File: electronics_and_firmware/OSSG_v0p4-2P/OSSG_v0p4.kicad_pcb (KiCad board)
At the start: 4 copper layers, 85 x 9 mm, 82 parts, among them J1 Conn_01x05_Male, J2 USB_B_Micro, Q1 2SC4617R BR, Q2 2SC4617R BR, Q3 PMZ290UNE2YL, Q4 EMF20B02V, SW1 SW_SPST, SW2 Power, U1 SPH0645LMH, U2 ESP32-PICO-D4, U3 CH9102F, U4 XC61CC3002MR, U5 MP2615CGQ-Z, U6 H7650-50PR, U7 NCP167BMX330TBG

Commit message: started work on PCB layout
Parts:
- removed C20: 1uF, Capacitor_SMD:C_0402_1005Metric
- removed D4: WS2812C-2020, OSSG_footprints:LED_WS2812C-2020
- removed D5, D6: LED, Diode_SMD:D_0402_1005Metric
- removed D7: RB160M-30, Diode_SMD:D_SOD-123
- removed JP1: SolderJumper_2_Open, OSSG_footprints:JUMPER-2Psml_Open_RoundedPad2x1mm
- removed R14: 160K, Resistor_SMD:R_0402_1005Metric
- removed R15, R19: 884K, Resistor_SMD:R_0402_1005Metric
- removed R16: 320K, Resistor_SMD:R_0402_1005Metric
- removed R17: .025, Resistor_SMD:R_0402_1005Metric
- removed R18, R20: 100K, Resistor_SMD:R_0402_1005Metric
- removed TH1: 10K, Connector_PinHeader_1.27mm:PinHeader_1x02_P1.27mm_Horizontal
- added J3: USB_B_Micro, Connector_USB:USB_Micro-B_Amphenol_10118194_Horizontal, F.Cu at (131.7, 81.3)
- added L1: 1.5uH, OSSG_footprints:1.5uH_YXMAA0402-1R5M-ANP, F.Cu at (140.3, 87.3)
- added TP18: BATT2-, OSSG_footprints:Breakout_pads, B.Cu at (156.5, 76.2)
- added TP19: 5V, OSSG_footprints:Breakout_pads_small, F.Cu at (148.4, 88.3)
- added U8: SY7088, Package_DFN_QFN:DFN-8-1EP_3x2mm_P0.5mm_EP1.7x1.4mm, F.Cu at (145.3, 89.3)
- C13: value 1uF/16V -> 100nF
- C14: value 1uF/16V -> 22uF/16V
- C15: value 100nF/16V -> 1uF
- C16: value 22uF/16V -> 100nF
- C17, C19: value 1uF -> 22uF
- C18: value 10uF -> 1uF
- D1: moved to B.Cu
- D2: value WS2812C-2020 -> Red; footprint OSSG_footprints:LED_WS2812C-2020 -> Diode_SMD:D_0402_1005Metric
- D3: value WS2812C-2020 -> RB160M-30; footprint OSSG_footprints:LED_WS2812C-2020 -> Diode_SMD:D_SOD-123
- J1: footprint Connector_PinHeader_1.00mm:PinHeader_1x05_P1.00mm_Horizontal -> Connector_PinHeader_1.00mm:PinHeader_1x05_P1.00mm_Vertical
- J2: value USB_B_Micro -> Ext RGB; footprint Connector_USB:USB_Micro-B_Amphenol_10118194_Horizontal -> Connector_PinHeader_1.00mm:PinHeader_1x03_P1.00mm_Vertical; moved to F.Cu
- Q4: footprint Package_TO_SOT_SMD:SOT-23-6 -> OSSG_footprints:EMF20B02V
- R10: value 100K -> 1M
- R11: value 442K -> 1M
- R12: value 442K -> 470K
- R13: value 160K -> 147K
- R7: value 10K -> 2K
- R8: value 2K -> 150
- R9: value 2K -> 100K
- TP1, TP10, TP11, TP2, TP3, TP4, TP6, TP7: moved to F.Cu
- TP12, TP5: footprint TestPoint:TestPoint_Pad_D1.0mm -> OSSG_footprints:Breakout_pads_small
- TP13, TP14: footprint TestPoint:TestPoint_Pad_D1.0mm -> OSSG_footprints:Breakout_pads_small; moved to F.Cu
- TP15: value Batt+ -> Batt1+
- TP16: value GND -> Batt2+
- TP17: value BattMid -> BATT1-
- TP8, TP9: footprint OSSG_footprints:Breakout_pads -> OSSG_footprints:Breakout_pads_small; moved to F.Cu
- U5: value MP2615CGQ-Z -> AP5054HTC; footprint OSSG_footprints:MP2615GQ-P -> Package_TO_SOT_SMD:SOT-23-6
- U6: value H7650-50PR -> MAX17048; footprint Package_TO_SOT_SMD:SOT-89-3 -> Package_DFN_QFN:DFN-8-1EP_2x2mm_P0.5mm_EP0.8x1.6mm
- moved TP13 81.6 mm to (76.1, 92.3), turned to 0 degrees
- moved TP14 78.7 mm to (79.2, 89.3), turned to 0 degrees
- moved U6 71.6 mm to (156.2, 77.5)
- moved R7 67.4 mm to (152.6, 80.2), turned to 180 degrees
- moved C15 66.4 mm to (148.8, 90.4)
- moved R1 64.8 mm to (86.0, 79.7), turned to 0 degrees
- moved C16 62.4 mm to (146.1, 87.4), turned to 180 degrees
- moved R6 61.8 mm to (148.0, 80.4), turned to 0 degrees
- moved D1 60.9 mm to (79.4, 76.7), turned to 0 degrees
- moved TP12 59.6 mm to (84.6, 89.3)
- moved TP5 59.6 mm to (81.5, 89.3)
- moved R3 55.3 mm to (96.7, 78.4)
- moved J1 52.3 mm to (79.6, 82.7), turned to 180 degrees
- moved TP4 49.3 mm to (74.0, 92.2), turned to 0 degrees
- moved J2 47.9 mm to (76.5, 76.2), turned to 0 degrees
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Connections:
- net IO4 renamed RGB
- C12 pad 1: BATT1- -> BATT+
- C13 pad 1: Net-(C13-Pad1) -> BATT+
- C14 pad 1: Net-(C14-Pad1) -> BATT+
- C15 pad 2: Net-(C15-Pad2) -> BATT2-
- C16 pad 1: BATT+ -> +5V
- C17 pad 1: V_PSU -> Net-(C15-Pad1)
- C18 pad 1: +5V -> BATT2-
- C18 pad 2: BATT2- -> +3V3
- C19 pad 1: BATT2- -> +5V
- C19 pad 2: V_PSU -> BATT2-
- D2 pad 2: BATT2- -> VBUS
- D3 pad 1: Net-(D3-Pad1) -> Net-(C15-Pad1)
- D3 pad 2: BATT2- -> VBUS
- J2 pad 1: V_USB -> BATT2-
- J2 pad 2: USB- -> Net-(D1-Pad1)
- J2 pad 3: USB+ -> +5V
- Q3 pad 1: PSEN -> Net-(Q3-Pad1)
- Q4 pad 3: V_PSU -> Net-(C15-Pad1)
- Q4 pad 4: V_USB -> VBUS
- R10 pad 1: BATT2- -> Net-(Q3-Pad3)
- R10 pad 2: Net-(R10-Pad2) -> BATT+
- R11 pad 1: BATT+ -> BATT2-
- R11 pad 2: Net-(R11-Pad2) -> VBUS
- R12 pad 1: Net-(R11-Pad2) -> Net-(R12-Pad1)
- R12 pad 2: ADC1C2 -> +5V
- R13 pad 1: ADC1C2 -> BATT2-
- R13 pad 2: Net-(R13-Pad2) -> Net-(R12-Pad1)
- R6 pad 1: BATT1- -> BATT+
- R7 pad 1: Net-(C13-Pad1) -> BATT2-
- R8 pad 1: Net-(D6-Pad1) -> PSEN
- R8 pad 2: Net-(R8-Pad2) -> Net-(Q3-Pad1)
- R9 pad 1: Net-(D5-Pad1) -> BATT2-
- R9 pad 2: Net-(R9-Pad2) -> Net-(Q3-Pad1)
- TP11 pad 1: IO18 -> unconnected-(TP11-Pad1)
- TP16 pad 1: BATT2- -> BATT+
- TP17 pad 1: BATT1- -> BATT2-
- TP2 pad 1: IO26 -> unconnected-(TP2-Pad1)
- TP6 pad 1: IO32 -> unconnected-(TP6-Pad1)
- U4 pad 3: BATT1- -> BATT+
- U5 pad 1: Net-(C15-Pad2) -> Net-(D2-Pad1)
- U5 pad 2: V_USB -> BATT2-
- U5 pad 3: Net-(R7-Pad2) -> BATT+
- U5 pad 4: Net-(JP1-Pad1) -> VBUS
- U5 pad 6: Net-(R10-Pad2) -> Net-(R7-Pad2)
- U6 pad 2: V_PSU -> BATT+
- U6 pad 3: +5V -> BATT+
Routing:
- net BATT2-: track 442.0 -> 0.01 mm, vias 73 -> 16
- net IO33: track 15.9 -> 0.00 mm, vias 2 -> 0
- net EN: track 15.0 -> 0.00 mm, vias 2 -> 0
- net ADC1C0: track 12.3 -> 0.00 mm, vias 1 -> 0
- net IO14: track 12.0 -> 0.00 mm, vias 3 -> 0
- net IO32: track 11.8 -> 0.00 mm, vias 3 -> 0
- net USB-: track 10.5 -> 0.00 mm
- net EXT1_MIC_DATA: track 9.77 -> 0.00 mm, vias 2 -> 0
- net IO5: track 6.86 -> 0.00 mm, vias 1 -> 0
- net Net-(R13-Pad2): track 5.83 -> 0.00 mm, vias 3 -> 0
- net ADC1C2: track 5.17 -> 0.00 mm, vias 2 -> 0
- net Net-(IC1-Pad3): track 4.96 -> 0.00 mm, vias 2 -> 0
- net Net-(C4-Pad1): track 4.69 -> 0.00 mm, vias 2 -> 0
- net Net-(IC1-Pad1): track 3.35 -> 0.00 mm
- net +3V3: track 3.19 -> 0.00 mm, vias 2 -> 0
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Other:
- outline, holes or cut-outs redrawn
- board text removed: "."

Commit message: V0.4-2P PCB nearly finished
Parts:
- removed TP11: IO18_BO, OSSG_footprints:Breakout_pads_small
- removed TP2: IO26_BO, OSSG_footprints:Breakout_pads_small
- removed TP6: IO32_BO, OSSG_footprints:Breakout_pads_small
- removed TP7: IO33_BO, OSSG_footprints:Breakout_pads_small
- added C20: 1uF, Capacitor_SMD:C_0402_1005Metric, F.Cu at (85.0, 77.9)
- added F1: 1A, Resistor_SMD:R_0805_2012Metric, F.Cu at (123.4, 76.9)
- added J4: Touch, OSSG_footprints:Solder-2P-Connector, B.Cu at (104.7, 84.4)
- added R14: 147K, Resistor_SMD:R_0402_1005Metric, F.Cu at (132.5, 76.1)
- C1: value 100nF -> 1uF
- C2: value 1uF -> 100nF
- C4: value 10uF -> 100nF
- C5: value 0.1uF -> 10uF
- J1: footprint Connector_PinHeader_1.00mm:PinHeader_1x05_P1.00mm_Vertical -> OSSG_footprints:Solder-5P-Connector; moved to B.Cu
- J2: footprint Connector_PinHeader_1.00mm:PinHeader_1x03_P1.00mm_Vertical -> OSSG_footprints:Solder-3P-Connector; moved to B.Cu
- R1: value 0R* -> 10K
- R10: value 1M -> 100K
- R12: value 470K -> 1M
- R13: value 147K -> 470K
- R3: value 10K -> 0R*
- R6: value 100k -> 10K
- R7: value 2K -> 100k
- R8: value 150 -> 2K
- R9: value 100K -> 150
- SW1: footprint Button_Switch_SMD:SW_SPST_B3U-3000P-B -> OSSG_footprints:SMD_Switch_Panasonic_EVQPUL_EVQPUC_6.3x6.7
- TP12: value IO0_TP -> IO0; footprint OSSG_footprints:Breakout_pads_small -> OSSG_footprints:Breakout_pads_very_small; moved to B.Cu
- TP13: value TXIN -> Tx; footprint OSSG_footprints:Breakout_pads_small -> OSSG_footprints:Breakout_pads_very_small; moved to B.Cu
- TP14: value RXIN -> Rx; footprint OSSG_footprints:Breakout_pads_small -> OSSG_footprints:Breakout_pads_very_small; moved to B.Cu
- TP19: moved to B.Cu
- TP5: footprint OSSG_footprints:Breakout_pads_small -> OSSG_footprints:Breakout_pads_very_small; moved to B.Cu
- TP8: value +3.3V_BO -> 3V3; moved to B.Cu
- TP9: value GND_BO -> GND; moved to B.Cu
- U1: value SPH0645LMH -> MP23DB01HPTR; footprint OSSG_footprints:SPH0645LM4H-B-SMD-GND -> OSSG_footprints:MP23DB01HPTR
- moved R4 47.4 mm to (77.0, 79.7)
- moved R6 40.7 mm to (107.2, 79.6), turned to 90 degrees
- moved TP13 34.6 mm to (107.3, 77.2), turned to 180 degrees
- moved TP14 30.4 mm to (106.6, 76.0), turned to 180 degrees
- moved C4 30.4 mm to (78.8, 79.7), turned to 0 degrees
- moved SW2 28.7 mm to (113.7, 80.3), turned to 0 degrees
- moved TP4 28.2 mm to (101.7, 87.4)
- moved C16 27.9 mm to (120.4, 76.6), turned to -90 degrees
- moved TP5 26.5 mm to (106.8, 81.1), turned to 180 degrees
- moved TP12 26.3 mm to (110.0, 82.5), turned to 180 degrees
- moved C15 22.9 mm to (130.1, 77.1), turned to 90 degrees
- moved C18 21.2 mm to (117.9, 76.6), turned to -90 degrees
- moved R13 21.1 mm to (131.1, 76.5), turned to 90 degrees
- moved TP1 20.4 mm to (104.3, 87.4)
- moved TP19 20.0 mm to (132.3, 76.4)
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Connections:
- C1 pad 1: +3V3 -> EN
- C2 pad 1: EN -> +3V3
- C4 pad 1: Net-(C4-Pad1) -> SWITCH
- C5 pad 1: Net-(C4-Pad1) -> +3V3
- C6 pad 1: ADC1C0 -> +3V3
- C7 pad 1: ADC1C1 -> ADC1C0
- C8 pad 1: ADC1C2 -> ADC1C1
- J1 pad 3: IO21 -> i2S2_CLK
- J1 pad 4: IO23 -> i2S2_Data
- J1 pad 5: IO9 -> i2S2_WS
- J3 pad 1: VBUS -> Net-(J3-Pad1)
- Q4 pad 5: Net-(Q4-Pad5) -> Net-(Q4-Pad6)
- Q4 pad 7: Net-(Q4-Pad5) -> Net-(Q4-Pad6)
- R1 pad 1: Net-(R1-Pad1) -> EN
- R10 pad 1: Net-(Q3-Pad3) -> BATT2-
- R10 pad 2: BATT+ -> Net-(Q3-Pad1)
- R11 pad 1: BATT2- -> Net-(Q3-Pad3)
- R11 pad 2: VBUS -> BATT+
- R12 pad 1: Net-(R12-Pad1) -> BATT2-
- R12 pad 2: +5V -> VBUS
- R13 pad 1: BATT2- -> Net-(R13-Pad1)
- R13 pad 2: Net-(R12-Pad1) -> +5V
- R2 pad 1: BATT2- -> Net-(R2-Pad1)
- R2 pad 2: Net-(R1-Pad1) -> +3V3
- R3 pad 1: EN -> BATT2-
- R3 pad 2: +3V3 -> Net-(R2-Pad1)
- R4 pad 1: DTR -> SWITCH
- R4 pad 2: Net-(Q1-Pad1) -> +3V3
- R5 pad 1: RTS -> DTR
- R5 pad 2: Net-(Q2-Pad1) -> Net-(Q1-Pad1)
- R6 pad 1: BATT+ -> RTS
- R6 pad 2: PSEN -> Net-(Q2-Pad1)
- R7 pad 1: BATT2- -> BATT+
- R7 pad 2: Net-(R7-Pad2) -> PSEN
- R8 pad 1: PSEN -> BATT2-
- R8 pad 2: Net-(Q3-Pad1) -> Net-(R8-Pad2)
- R9 pad 1: BATT2- -> PSEN
- SW1 pad 1: BATT2- -> SWITCH
- SW1 pad 2: EN -> BATT2-
- U1 pad 1: IO33 -> i2S1_Data
- U1 pad 2: Net-(R1-Pad1) -> Net-(R2-Pad1)
- U1 pad 4: IO32 -> i2S1_CLK
- U1 pad 6: IO14 -> (no net)
- U2 pad 12: IO32 -> i2S2_WS
- U2 pad 13: IO33 -> i2S1_CLK
- U2 pad 14: IO25 -> i2S2_CLK
- U2 pad 15: IO26 -> i2S1_Data
- U2 pad 16: IO27 -> unconnected-(U2-Pad16)
- U2 pad 17: IO14 -> RGB
- U2 pad 22: IO2 -> TOUCH1
- U2 pad 24: RGB -> SDA
- U2 pad 35: IO18 -> SCL
- U2 pad 36: IO23 -> unconnected-(U2-Pad36)
- U2 pad 42: IO21 -> ALRT
- U2 pad 5: ADC1C2 -> SWITCH
- U2 pad 6: ADC1C0 -> unconnected-(U2-Pad6)
- U2 pad 8: IO39 -> i2S2_Data
- U5 pad 6: Net-(R7-Pad2) -> Net-(R8-Pad2)
- U6 pad 5: IO18 -> ALRT
- U6 pad 7: IO32 -> SCL
- U6 pad 8: IO26 -> SDA
- U8 pad 5: Net-(R12-Pad1) -> Net-(R13-Pad1)
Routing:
- net +5V: track 0.00 -> 77.1 mm, vias 0 -> 7
- net BATT2-: track 0.01 -> 76.0 mm, vias 16 -> 93
- net SCL: track 0.00 -> 60.8 mm, vias 0 -> 2
- net ALRT: track 0.00 -> 59.3 mm, vias 0 -> 2
- net SDA: track 0.00 -> 54.5 mm, vias 0 -> 2
- net VBUS: track 0.00 -> 53.5 mm, vias 0 -> 6
- net PSEN: track 0.00 -> 47.1 mm, vias 0 -> 4
- net BATT+: track 0.20 -> 33.5 mm, vias 0 -> 3
- net SWITCH: track 0.00 -> 27.0 mm, vias 0 -> 2
- net +3V3: track 0.00 -> 26.6 mm, vias 0 -> 17
- net Net-(C15-Pad1): track 0.00 -> 23.9 mm, vias 0 -> 2
- net RGB: track 0.00 -> 22.8 mm, vias 0 -> 3
- net USB+: track 0.00 -> 22.0 mm, vias 0 -> 2
- net USB-: track 0.00 -> 20.5 mm, vias 0 -> 2
- net i2S1_Data: track 0.00 -> 20.0 mm, vias 0 -> 2
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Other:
- outline, holes or cut-outs redrawn
- board text added: "+"
- board text added: "-"
- board text added: "3V3"
- board text added: "5V"
- board text added: "CLK"
- board text added: "D"
- board text added: "Din"
- board text added: "GND"
- board text added: "OFF"
- board text added: "ON"
- board text added: "Open Source Smart Glasses v0.4"
- board text added: "Power OFF<-->ON"
- board text added: "USB DATA POWER"
- board text added: "WS"
- board text removed: "Open Source Smart Glasses v0.3"

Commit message: EOD - PCB nearly finished
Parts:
- removed C7, C8: 0.1uF, Capacitor_SMD:C_0402_1005Metric
- removed TP10: IO5_BO, OSSG_footprints:Breakout_pads_small
- removed TP19: 5V, OSSG_footprints:Breakout_pads_small
- removed TP3: IO38_ADC1C1, OSSG_footprints:Breakout_pads_small
- removed TP4: IO37_ADC1C0, OSSG_footprints:Breakout_pads_small
- added R15: 10K, Resistor_SMD:R_0402_1005Metric, F.Cu at (132.9, 82.8)
- added R16: 10k, Resistor_SMD:R_0402_1005Metric, F.Cu at (134.0, 82.8)
- added R17: 10K, Resistor_SMD:R_0402_1005Metric, F.Cu at (135.0, 82.7)
- added R18: 100K, Resistor_SMD:R_0402_1005Metric, F.Cu at (120.6, 78.7)
- added TP2: 5V, OSSG_footprints:Breakout_pads_small, B.Cu at (132.2, 76.4)
- TP1: value IO25_BO -> IO35; footprint OSSG_footprints:Breakout_pads_small -> OSSG_footprints:Breakout_pads_very_small; moved to B.Cu
- moved TP1 8.68 mm to (97.9, 81.5), turned to 180 degrees
- moved TP13 0.09 mm to (107.2, 77.2)
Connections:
- net BATT+ renamed BATT1+
- net BATT2- renamed BATT1-
- C9 pad 2: V_USB -> VBUS
- SW2 pad 2: PSEN -> Net-(Q3-Pad1)
- SW2 pad 3: unconnected-(SW2-Pad3) -> Net-(SW2-Pad3)
- TP1 pad 1: IO25 -> SPARE
- U2 pad 10: IO34 -> unconnected-(U2-Pad10)
- U2 pad 11: IO35 -> SPARE
- U2 pad 18: IO12 -> unconnected-(U2-Pad18)
- U2 pad 20: IO13 -> unconnected-(U2-Pad20)
- U2 pad 21: IO15 -> unconnected-(U2-Pad21)
- U2 pad 28: IO9 -> unconnected-(U2-Pad28)
- U2 pad 34: IO5 -> unconnected-(U2-Pad34)
- U2 pad 38: IO19 -> unconnected-(U2-Pad38)
- U2 pad 39: IO22 -> unconnected-(U2-Pad39)
- U2 pad 7: ADC1C1 -> unconnected-(U2-Pad7)
- U3 pad 7: V_USB -> VBUS
- U3 pad 8: V_USB -> VBUS
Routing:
- net BATT1+: track 33.5 -> 53.5 mm, vias 3 -> 4
- net VBUS: track 53.5 -> 70.0 mm, vias 6 -> 7
- net +3V3: track 26.6 -> 29.8 mm, vias 17 -> 18
- net SDA: track 54.5 -> 57.0 mm, vias 2 -> 4
- net V_USB: track 2.05 -> 0.00 mm
- net SPARE: track 0.00 -> 1.69 mm, vias 0 -> 1
- net ALRT: track 59.3 -> 60.9 mm, vias 2 -> 3
- net SCL: track 60.8 -> 62.3 mm, vias 2 -> 3
- net Net-(SW2-Pad3): track 0.00 -> 1.23 mm
- net +5V: track 77.1 -> 78.0 mm
- net BATT1-: vias 93 -> 101
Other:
- outline, holes or cut-outs redrawn
- board text added: "Open Source Smart Glasses V0.4"
- board text removed: "Open Source Smart Glasses v0.4"

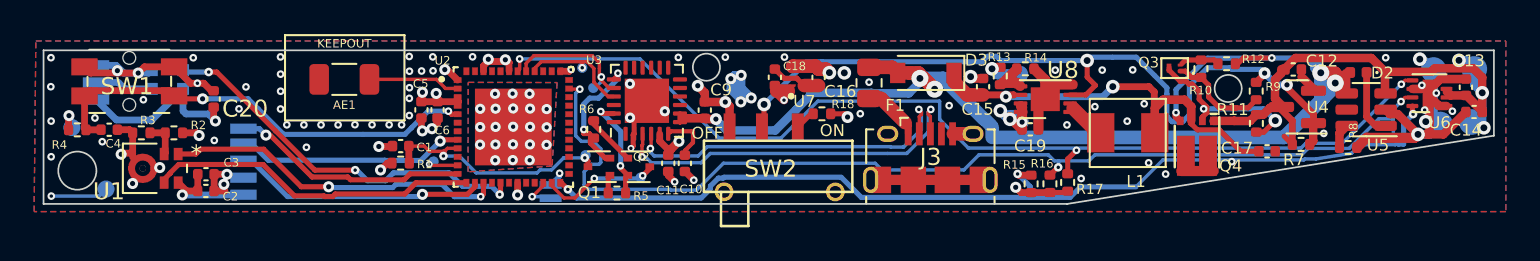
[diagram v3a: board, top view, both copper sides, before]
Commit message: V0.4 PCB nearly finished.  3D models mostly added in. Needs reviewing
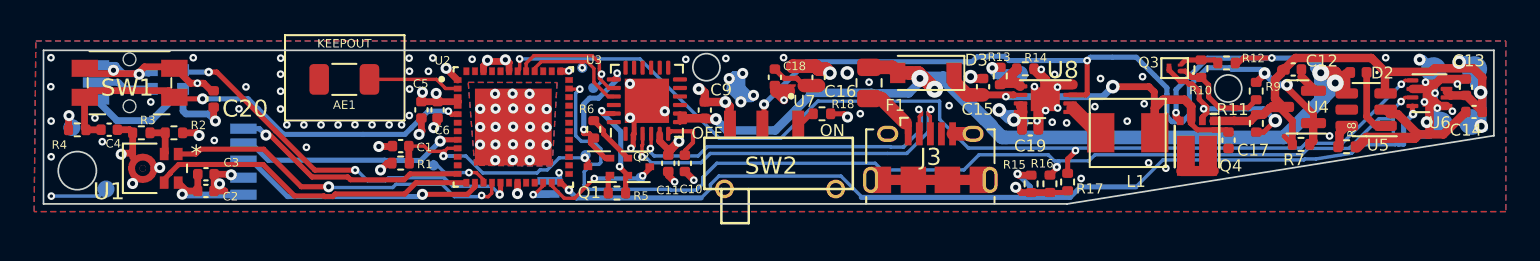
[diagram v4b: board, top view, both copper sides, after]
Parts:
- R18: value 100K -> 10K
- TP1: value IO35 -> IO26
- moved C17 2.35 mm to (144.4, 80.3), turned to -90 degrees
- moved J4 0.27 mm to (104.6, 84.1)
- moved TP1 0.23 mm to (97.9, 81.7)
- moved SW2 0.17 mm to (113.7, 80.1)
- moved R8 0.11 mm to (151.4, 80.7)
- moved SW1 0.08 mm to (80.0, 76.9)
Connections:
- net BATT1+ renamed BATT+
- SW2 pad 2: Net-(Q3-Pad1) -> PSEN
- TP1 pad 1: SPARE -> DAC
- U2 pad 15: i2S1_Data -> DAC
- U2 pad 16: unconnected-(U2-Pad16) -> i2S1_Data
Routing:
- net BATT+: track 53.5 -> 79.1 mm
- net DAC: track 0.00 -> 3.54 mm, vias 0 -> 1
- net +5V: track 78.0 -> 75.8 mm, vias 7 -> 6
- net Net-(C15-Pad1): track 23.9 -> 22.1 mm
- net SPARE: track 1.69 -> 0.00 mm, vias 1 -> 0
- net BATT1-: track 76.0 -> 77.1 mm, vias 101 -> 107
- net EN: track 14.0 -> 15.0 mm
- net TOUCH1: track 2.20 -> 3.08 mm
- net SDA: track 57.0 -> 57.2 mm, vias 4 -> 3

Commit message: finished board?
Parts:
- TP5: value EN_TP -> EN
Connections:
- SW2 pad 2: PSEN -> Net-(Q3-Pad1)
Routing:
- net +3V3: track 29.7 -> 39.2 mm
- net VBUS: track 69.6 -> 63.3 mm
- net PSEN: track 46.7 -> 42.1 mm
- net +5V: track 75.8 -> 75.1 mm
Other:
- board text added: "LED"
- board text added: "Power ON<-->OFF"
- board text added: "Touch"
- board text added: "i2S"
- board text removed: "Power OFF<-->ON"

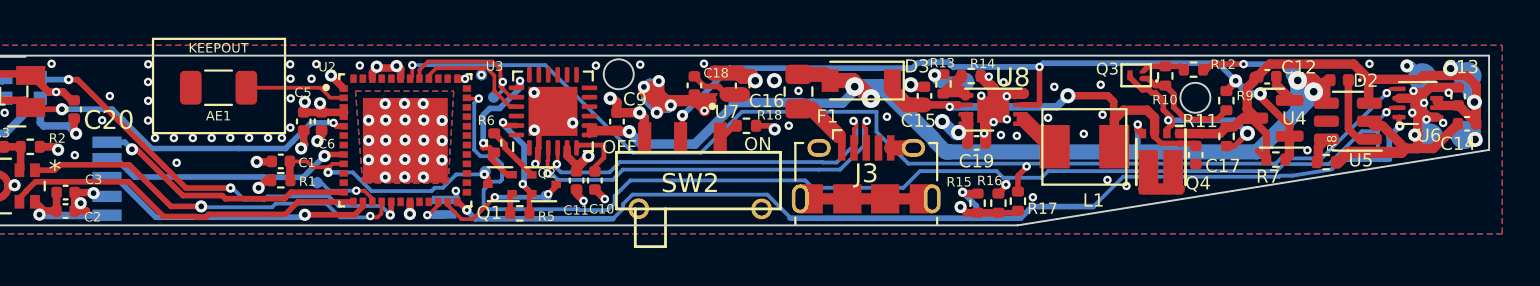
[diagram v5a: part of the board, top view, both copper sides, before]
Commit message: minor footprint updates
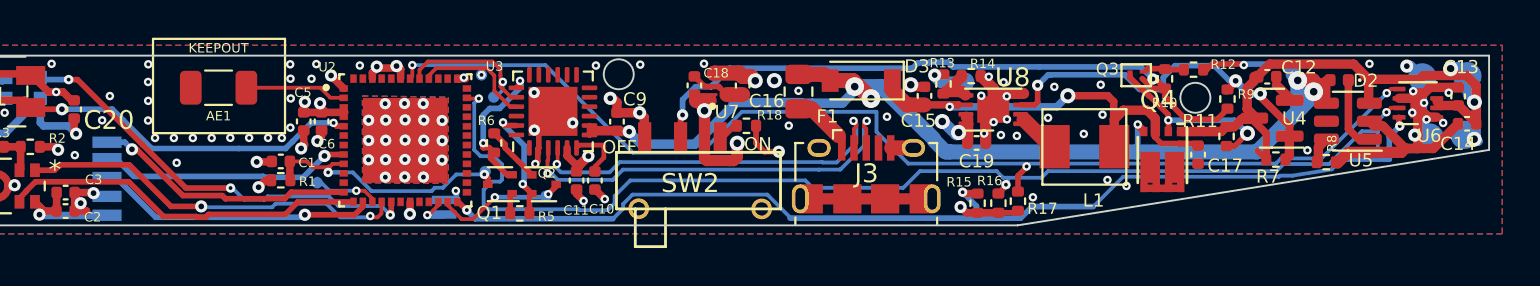
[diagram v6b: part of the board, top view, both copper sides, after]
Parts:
- moved R10 0.16 mm to (142.8, 76.2)
- moved Q4 0.13 mm to (142.6, 80.4)
- moved C17 0.12 mm to (144.6, 80.3)
- moved R9 0.10 mm to (146.1, 77.3)
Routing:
- net Net-(Q3-Pad1): track 6.09 -> 35.6 mm, vias 0 -> 2
- net PSEN: track 42.1 -> 20.7 mm, vias 4 -> 3
- net +3V3: track 39.2 -> 32.4 mm, vias 18 -> 15
- net +5V: track 75.1 -> 79.1 mm
- net Net-(Q3-Pad3): track 10.5 -> 9.76 mm

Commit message: update Readme with board change info
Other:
- board text added: "M1.5"
- board text added: "M2.25"
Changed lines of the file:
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@@
     (property "Sheetname" "")
     (attr through_hole)
-    (fp_text reference "J4" (at -2.140698 0.098015 180) (layer "B.SilkS")
+    (fp_text reference "J4" (at -1.979542 -0.115966 180) (layer "B.SilkS")
       (effects (font (size 0.5 0.5) (thickness 0.07)) (justify mirror))
     )
@@
     (effects (font (size 0.7 0.7) (thickness 0.12)) (justify mirror))
   )
+  (gr_text "M1.5" (at 144.426825 75.859363) (layer "B.SilkS")
+    (effects (font (size 0.7 0.7) (thickness 0.12)) (justify mirror))
+  )
   (gr_text "+" (at 159.662503 75.316457) (layer "B.SilkS")
     (effects (font (size 0.5 0.5) (thickness 0.125)) (justify mirror))
@@
   )
   (gr_text "GND" (at 88.58336 82.480347) (layer "B.SilkS")
+    (effects (font (size 0.7 0.7) (thickness 0.12)) (justify mirror))
+  )
+  (gr_text "M1.5" (at 116.03365 76.242806) (layer "B.SilkS")
+    (effects (font (size 0.7 0.7) (thickness 0.12)) (justify mirror))
+  )
+  (gr_text "M2.25" (at 79.571708 81.059996) (layer "B.SilkS")
     (effects (font (size 0.7 0.7) (thickness 0.12)) (justify mirror))
   )
@@
     )
   )
-  (zone (net 0) (net_name "") (layer "B.Mask") (hatch edge 0.508)
+  (zone (net 0) (net_name "") (layers "B.Paste" "B.Mask") (hatch edge 0.508)
     (connect_pads (clearance 0.05))
     (min_thickness 0.254) (filled_areas_thickness no)
@@
     (polygon
       (pts
-        (xy 104.865435 81.79807)
-        (xy 100.214026 81.79807)
+        (xy 104.866543 81.385302)
+        (xy 104.443911 81.801263)
+        (xy 100.639247 81.801212)
+        (xy 100.220006 81.373362)
         (xy 100.242828 77.153862)
         (xy 104.822234 77.182663)
